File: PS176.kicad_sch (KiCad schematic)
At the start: 45 parts, among them U12 PS176, U14 TLV62568DBVR, X4 27MHz 8pF 50Ω

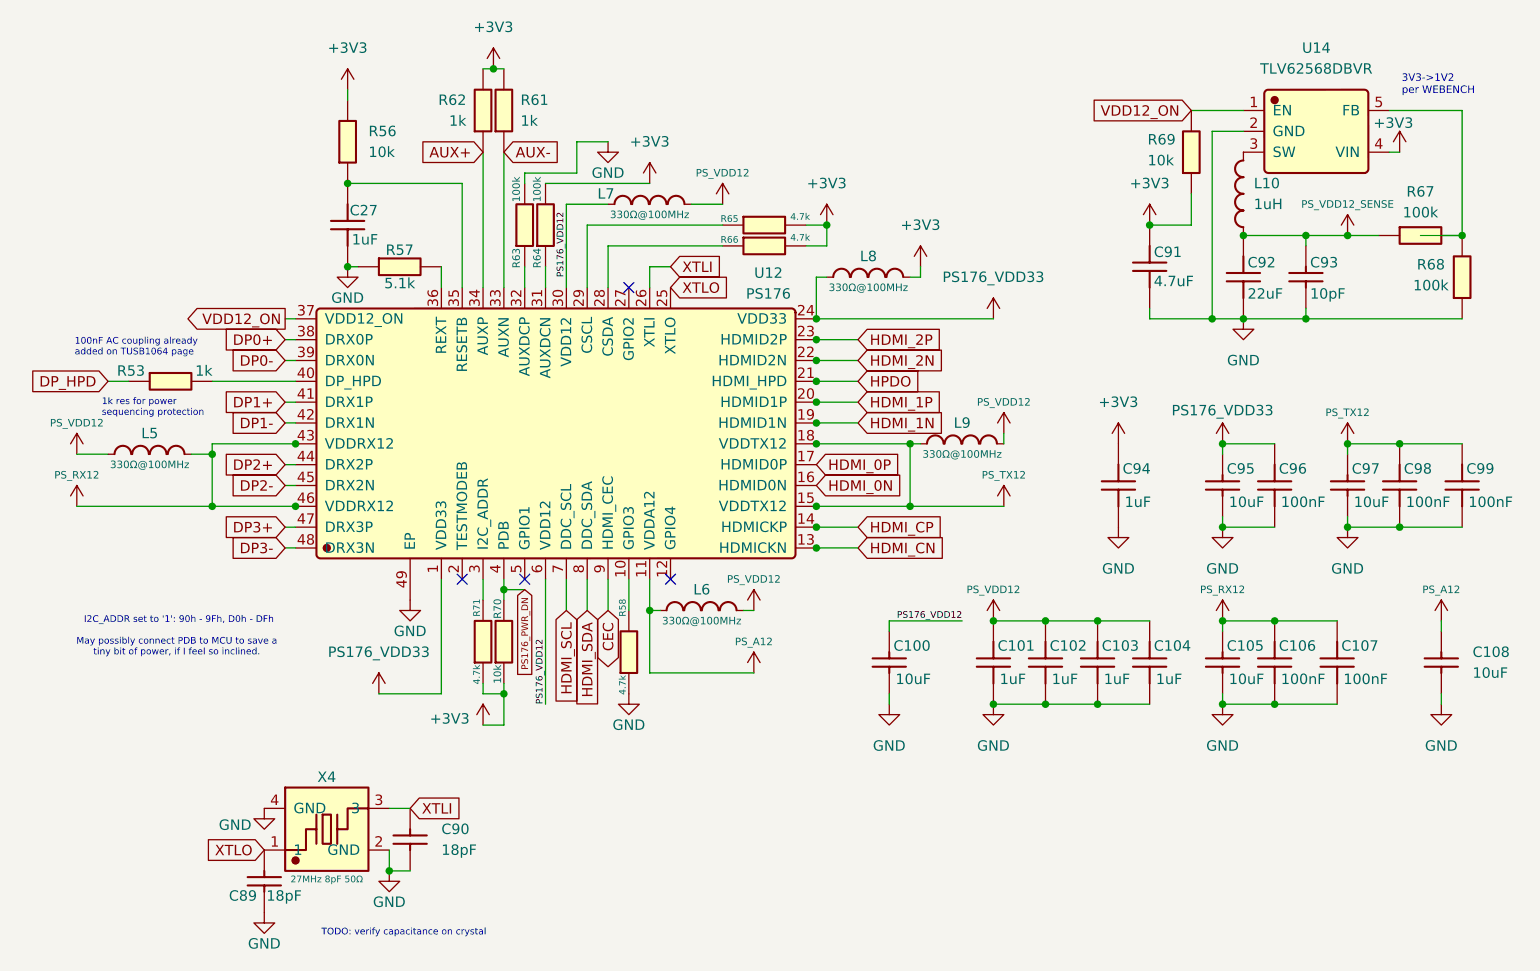
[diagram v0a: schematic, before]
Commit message: Mostly complete initial transfer to hierarchical schematic
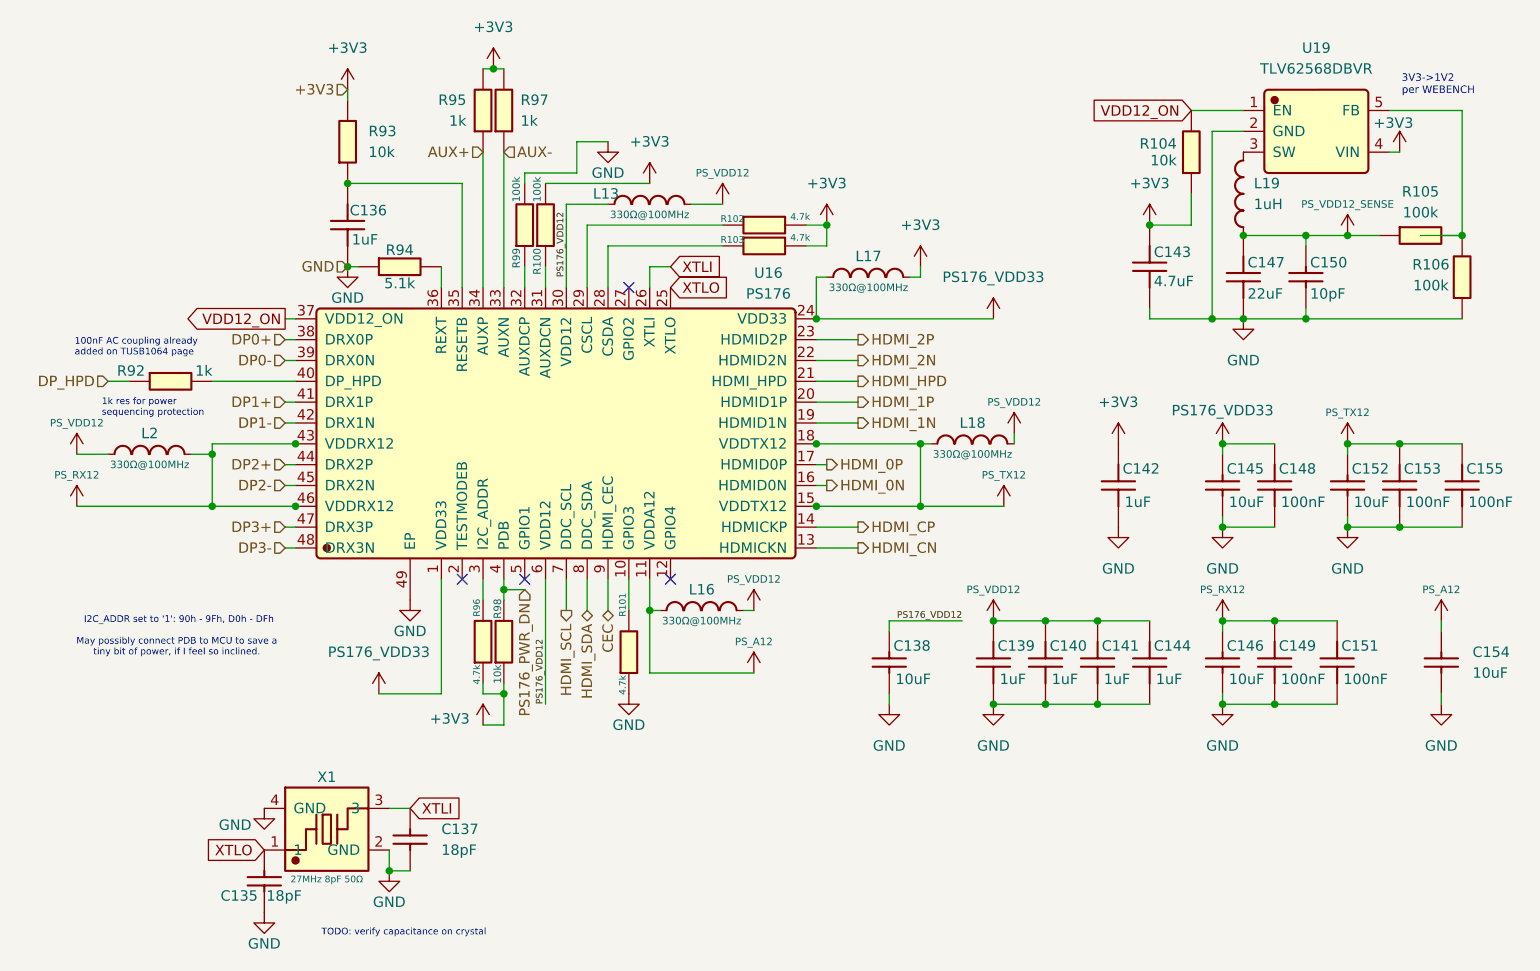
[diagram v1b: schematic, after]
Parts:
- renumbered C89 to C135, C27 to C136, C90 to C137, C100 to C138, C101 to C139, C102 to C140, C103 to C141, C94 to C142, C91 to C143, C104 to C144, C95 to C145, C105 to C146, C92 to C147, C96 to C148, C106 to C149, C93 to C150, C107 to C151, C97 to C152, C98 to C153, C108 to C154, C99 to C155, L7 to L13, L6 to L16, L8 to L17, L9 to L18, L10 to L19, L5 to L2, R64 to R100, R58 to R101, R65 to R102, R66 to R103, R69 to R104, R67 to R105, R68 to R106, R53 to R92, R56 to R93, R57 to R94, R62 to R95, R71 to R96, R61 to R97, R70 to R98, R63 to R99, U12 to U16, U14 to U19, X4 to X1
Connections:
- net HPDO renamed HDMI_HPD
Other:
- moved on the sheet: L18

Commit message: Cleaned up PS176 schematic and added some datasheets
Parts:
- removed C143: 4.7uF, Capacitor_SMD:C_0603_1608Metric, symbol JLCImport:CL10A475KO8NNNC
- removed C147: 22uF, Capacitor_SMD:C_0603_1608Metric, symbol JLCImport:CL10A226MQ8NRNC
- removed C150: 10pF, Capacitor_SMD:C_0603_1608Metric, symbol JLCImport:CL10C100JB8NNNC
- removed L19: 1uH, TerminalBlock_Phoenix:TerminalBlock_Phoenix_PTSM-0,5-2-2,5-V-SMD_1x02-1MP_P2.50mm_Vertical, symbol JLCImport:FTC252012S1R0MBCA
- removed R104: 10k, Resistor_SMD:R_0402_1005Metric, symbol JLCImport:0402WGF1002TCE
- removed R105, R106: 100k, Resistor_SMD:R_0402_1005Metric, symbol JLCImport:0402WGF1003TCE
- removed U19: TLV62568DBVR, JLCImport:TLV62568DBVR, symbol JLCImport:TLV62568DBVR
- added C318, C320: 4.7uF, Capacitor_SMD:C_0402_1005Metric, symbol JLCImport:CL05A475MP5NRNC
- added C319: 100nF, Capacitor_SMD:C_0402_1005Metric, symbol JLCImport:CL05B104KB54PNC
- added L21: 4.7uH, JLCImport:PIM201608S4R7MBCA, symbol JLCImport:PIM201608S4R7MBCA
- added R388: 10.0, Resistor_SMD:R_0402_1005Metric, symbol JLCImport:0402WGF100JTCE
- added R389: 10k, Resistor_SMD:R_0402_1005Metric, symbol JLCImport:0402WGF1002TCE
- added U70: MCP1602-120I_MF, JLCImport:MCP1602-120I_MF, symbol JLCImport:MCP1602-120I_MF
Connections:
- net GND: now also C318.1, C319.1, C320.1, U70.4 (AGND), U70.8 (PGND), U70.9 (EP)
- net VDD12_ON: now also U70.1 (SHDN#)
- net PS176_VDD12 renamed V12
- net PS176_VDD33 renamed V33
- net PS_A12 renamed A12
- net PS_RX12 renamed RX12
- net PS_TX12 renamed TX12
- net PS_VDD12 renamed VDD12
- net VDD12: now also C320.2, L21.2, U70.5 (VOUT/VFB)
- new net: L21.1, U70.7 (LX)
- new net: C319.2, R388.1, U70.2 (VCC)
- new net: R389.2, U70.3 (PG)
- new net +3V3_CSI: C318.2, R388.2, R389.1, U70.6 (VIN)
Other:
- note removed: "3V3->1V2 per WEBENCH"
- moved on the sheet: C135, C137, C138, L17

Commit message: Basic function review and documentation for PS176 subsystem
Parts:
- removed C135, C137: 18pF, Capacitor_SMD:C_0402_1005Metric, symbol JLCImport:0402CG180J500NT
- removed X1: 27MHz 8pF 50Ω, JLCImport:5YMA27000121IF50E1, symbol JLCImport:5YMA27000121IF50E1
- added C143: 10uF, Capacitor_SMD:C_0402_1005Metric, symbol JLCImport:CL05A106MQ5NUNC
- added C150: 100nF, Capacitor_SMD:C_0402_1005Metric, symbol JLCImport:CL05B104KB54PNC
- added C314, C48: 10pF, Capacitor_SMD:C_0603_1608Metric, symbol JLCImport:CL10C100JB8NNNC
- added R29, R30: 2k, Resistor_SMD:R_0402_1005Metric, symbol JLCImport:1RC0402J0202
- added Y2: 27MHz 9pF, Crystal:Crystal_SMD_3225-4Pin_3.2x2.5mm, symbol Device:Crystal_GND24
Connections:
- net +3V3_CSI is gone; now on net +3V3: C318.2, R388.2, R389.1, U70.6 (VIN)
- net GND: now also C143.1, C150.1, C314.2, C48.1, Y2.2 (G), Y2.4 (G)
- net HDMI_SCL: now also R30.1
- net HDMI_SDA: now also R29.1
- net XTLI: now also C314.1, Y2.3
- net XTLO: now also C48.2, Y2.1
- new net +5V: C143.2, C150.2, R29.2, R30.2
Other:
- note removed: "TODO: verify capacitance on crystal"
- moved on the sheet: C138, C139, C140, C141, C144, C146, C149, C151

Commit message: Basic Function Review and Documentation for TUSB1064 subsystem
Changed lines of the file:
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@@
 	)
 	(hierarchical_label "AUX-"
-		(shape input)
+		(shape bidirectional)
 		(at 72.39 29.21 0)
 		(effects
@@
 	)
 	(hierarchical_label "DP_HPD"
-		(shape input)
+		(shape output)
 		(at 24.13 57.15 180)
 		(effects
@@
 	)
 	(hierarchical_label "AUX+"
-		(shape input)
+		(shape bidirectional)
 		(at 69.85 29.21 180)
 		(effects
@@
 	)
 	(hierarchical_label "HDMI_HPD"
-		(shape output)
+		(shape input)
 		(at 115.57 57.15 0)
 		(effects

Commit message: Small bug fixes to LT6911C subsystem to match official adapter model
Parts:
- removed L13, L18: 330Ω@100MHz, JLCImport:BLM18KG331SN1D, symbol JLCImport:BLM18KG331SN1D
- added DNP1: 1M, Resistor_SMD:R_0402_1005Metric, symbol Device:R
- added L18, L20: 120Ω@100MHz, Inductor_SMD:L_0805_2012Metric, symbol JLCImport:GDPZ2012M121-4A0TF
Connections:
- net TX12: now also L18.1
- net V12: now also L20.1
- net VDD12: now also L18.2, L20.2
- net XTLI: now also DNP1.2
- net XTLO: now also DNP1.1

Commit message: Basic Function Review/Documentation for LT6911C Subsystem
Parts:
- removed L17, L2: 330Ω@100MHz, JLCImport:BLM18KG331SN1D, symbol JLCImport:BLM18KG331SN1D
- added L22, L23: 120Ω@100MHz, Inductor_SMD:L_0805_2012Metric, symbol JLCImport:GDPZ2012M121-4A0TF
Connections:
- net +3V3: now also L22.2
- net RX12: now also L23.2
- net V33: now also L22.1
- net VDD12: now also L23.1
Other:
- moved on the sheet: R29, R30
